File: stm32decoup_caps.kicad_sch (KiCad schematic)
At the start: 15 parts

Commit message: adding connectors for display and pi power, pin headers
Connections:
- net VDD renamed 3V3_MCU
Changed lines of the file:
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@@
     (stroke (width 0) (type default))
   )
-  (wire (pts (xy 29.21 39.37) (xy 29.21 40.64))
+  (wire (pts (xy 26.67 39.37) (xy 26.67 40.64))
     (stroke (width 0) (type default))
   )
@@
   )
   (wire (pts (xy 54.61 52.07) (xy 44.45 52.07))
+    (stroke (width 0) (type default))
+  )
+  (wire (pts (xy 26.67 40.64) (xy 29.21 40.64))
     (stroke (width 0) (type default))
   )
@@
     )
   )
-  (global_label "VOUT2" (shape bidirectional) (at 29.21 39.37 180) (fields_autoplaced)
+  (global_label "3V3_MCU" (shape bidirectional) (at 26.67 39.37 180) (fields_autoplaced)
     (effects (font (size 1.27 1.27)) (justify right))
-    (property "Intersheetrefs" "${INTERSHEET_REFS}" (at 19.1868 39.37 0)
+    (property "Intersheetrefs" "${INTERSHEET_REFS}" (at 14.0464 39.37 0)
       (effects (font (size 1.27 1.27)) (justify right) hide)
     )

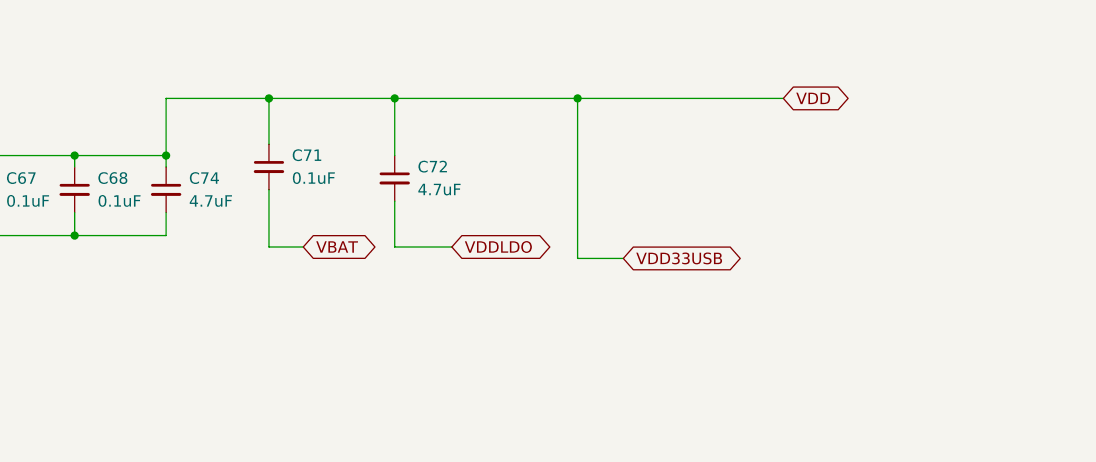
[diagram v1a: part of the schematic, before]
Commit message: changing sizes of caps from 06 to 04, also using vias on DW spi interfact to stm32
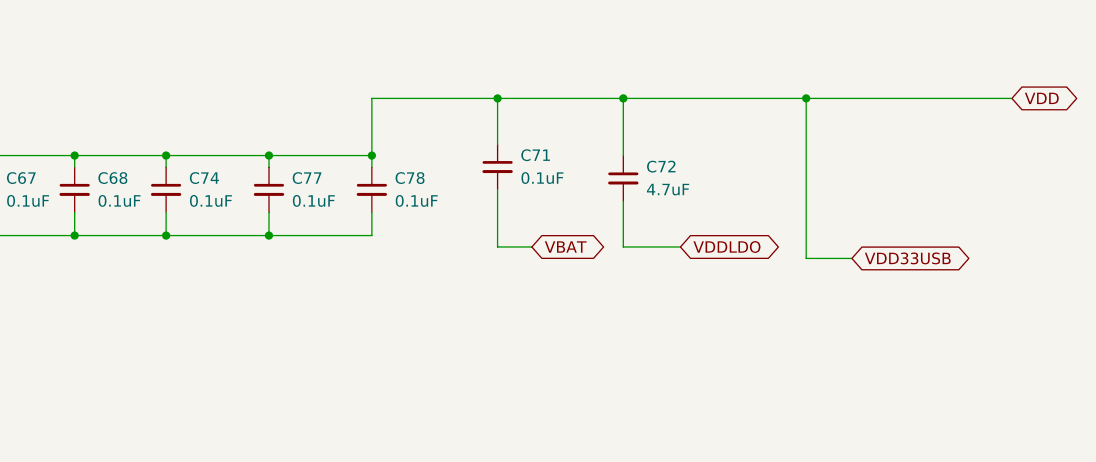
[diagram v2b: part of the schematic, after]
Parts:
- added C77, C78: 0.1uF, Capacitor_SMD:C_0402_1005Metric, symbol Device:C_Small
- C59, C60, C61, C62, C63, C64, C65, C66, C67, C68, C69, C70, C71, C72: footprint Capacitor_SMD:C_0603_1608Metric -> Capacitor_SMD:C_0402_1005Metric
- C74: value 4.7uF -> 0.1uF; footprint Capacitor_SMD:C_0603_1608Metric -> Capacitor_SMD:C_0402_1005Metric
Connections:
- net 3V3_MCU: now also C77.1, C78.1
- net GND: now also C77.2, C78.2
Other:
- moved on the sheet: C71, C72
